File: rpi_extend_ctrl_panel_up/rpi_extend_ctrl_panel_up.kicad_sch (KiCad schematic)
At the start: 54 parts, among them J1 Raspberry_Pi_2_3, Q1 BC547, Q2 BC547, SW1 E-SWITCH-SW_Push_LED, SW2 RotaryEncoder, SW3 E-SWITCH-SW_Push_LED, SW4 RotaryEncoder, SW5 RotaryEncoder_Switch, SW6 on panel, U1 74HC14, U2 lcd_16x2_i2c

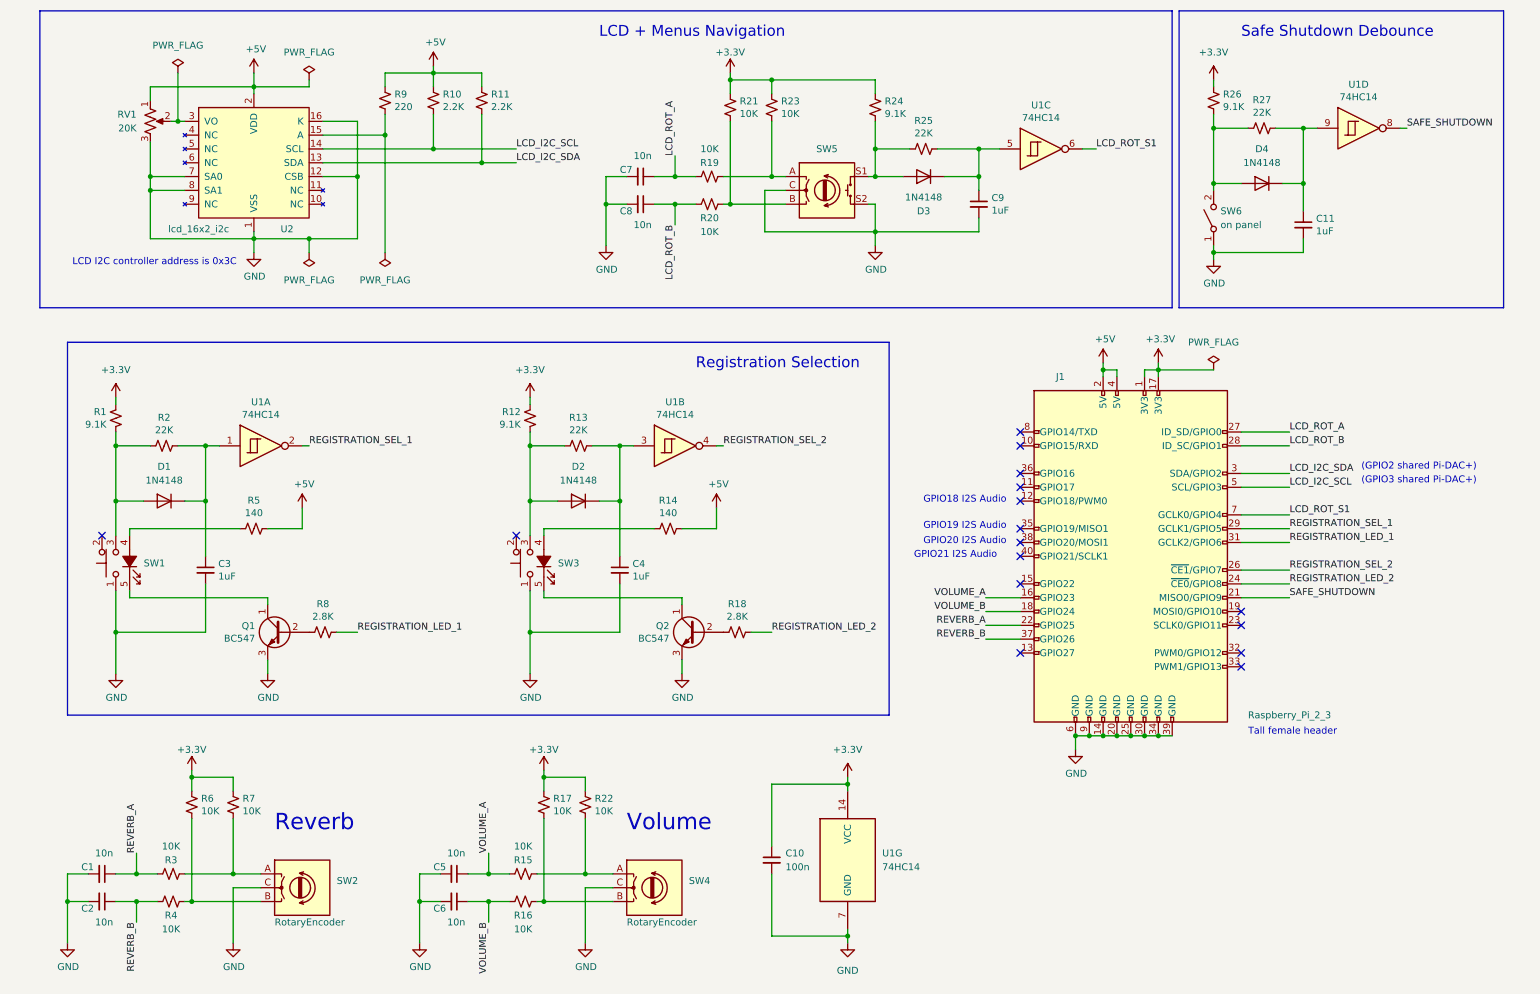
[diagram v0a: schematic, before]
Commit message: Rev 1.1: I2C pull-ups modified
SDA and SCL external pups (R10 and R11) discarded. Use Raspberry PI internal pups instead. Updating the PCB is not necessary.
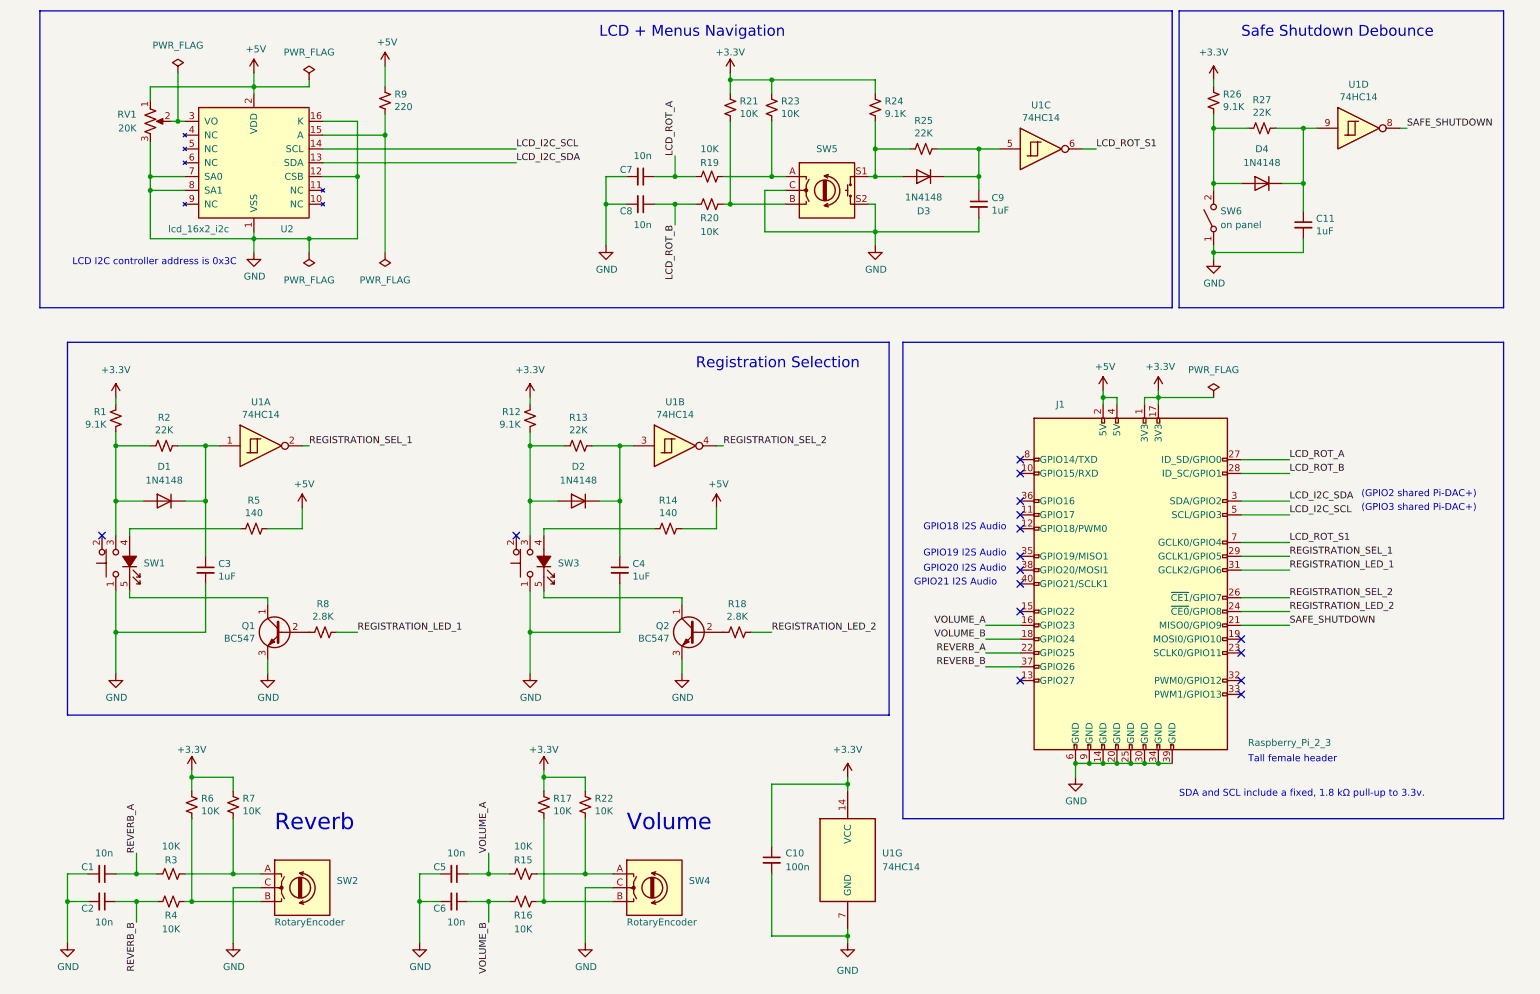
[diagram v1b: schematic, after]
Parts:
- removed R10, R11: 2.2K, Resistor_SMD:R_1206_3216Metric_Pad1.30x1.75mm_HandSolder, symbol Device:R_Small_US
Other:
- note added: "SDA and SCL include a fixed, 1.8 kΩ pull-up to 3.3v."
- moved on the sheet: J1

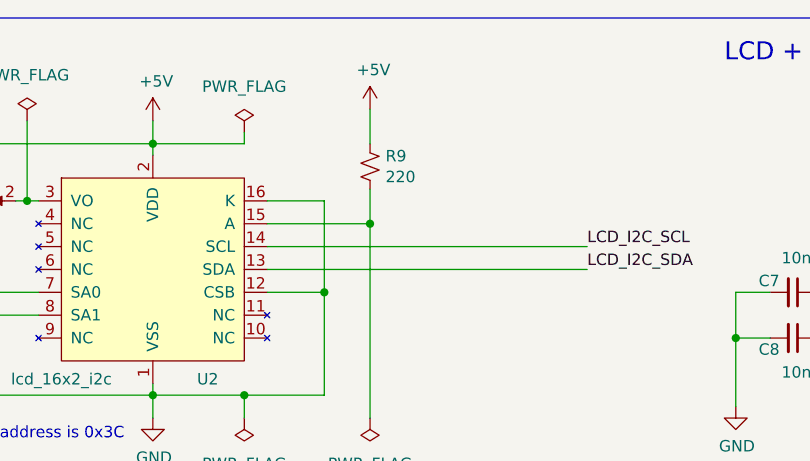
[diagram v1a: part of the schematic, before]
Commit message: Rev 1.1
I2C pull-ups discarded (use RPI I2C GPIO internal pull-ups). R9 value set to 51 Ohm.
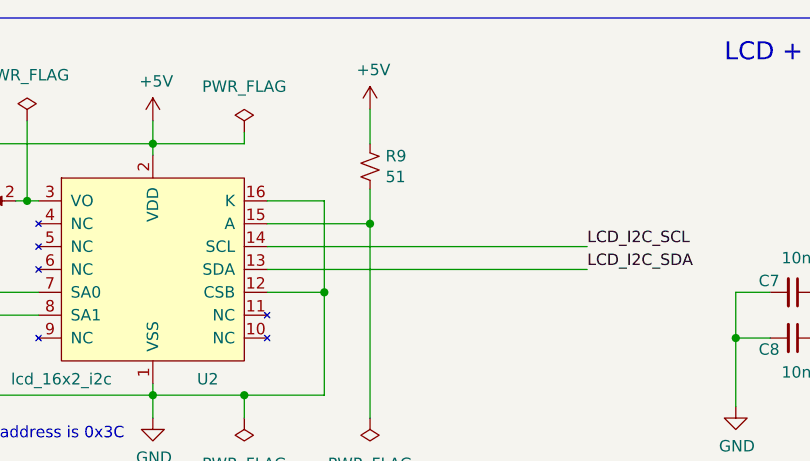
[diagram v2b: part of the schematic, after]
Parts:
- R9: value 220 -> 51
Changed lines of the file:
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@@
     (rev "1.1")
     (company "Picherie")
-    (comment 1 "Rev 1.1: SDA and SCL external pups (R10 and R11) discarded. Use Rpi internal pups instead.")
+    (comment 1 "SDA and SCL external pups (R10 and R11) discarded. Use Rpi internal pups instead.")
+    (comment 2 "R9 = 220 replaced with 51")
   )
   (junction (at 118.11 49.53) (diameter 0) (color 0 0 0 0)
@@
       (effects (font (size 1.27 1.27)) (justify left))
     )
-    (property "Value" "220" (id 1) (at 79.1972 31.623 0)
+    (property "Value" "51" (id 1) (at 79.1972 31.623 0)
       (effects (font (size 1.27 1.27)) (justify left))
     )
@@
     )
     (path "/00000000-0000-0000-0000-000061ba4973"
-      (reference "R9") (unit 1) (value "220") (footprint "Resistor_SMD:R_1206_3216Metric_Pad1.30x1.75mm_HandSolder")
+      (reference "R9") (unit 1) (value "51") (footprint "Resistor_SMD:R_1206_3216Metric_Pad1.30x1.75mm_HandSolder")
     )
     (path "/a9f36509-ce44-4e7e-bf3d-d4d8c7f2a8d8"

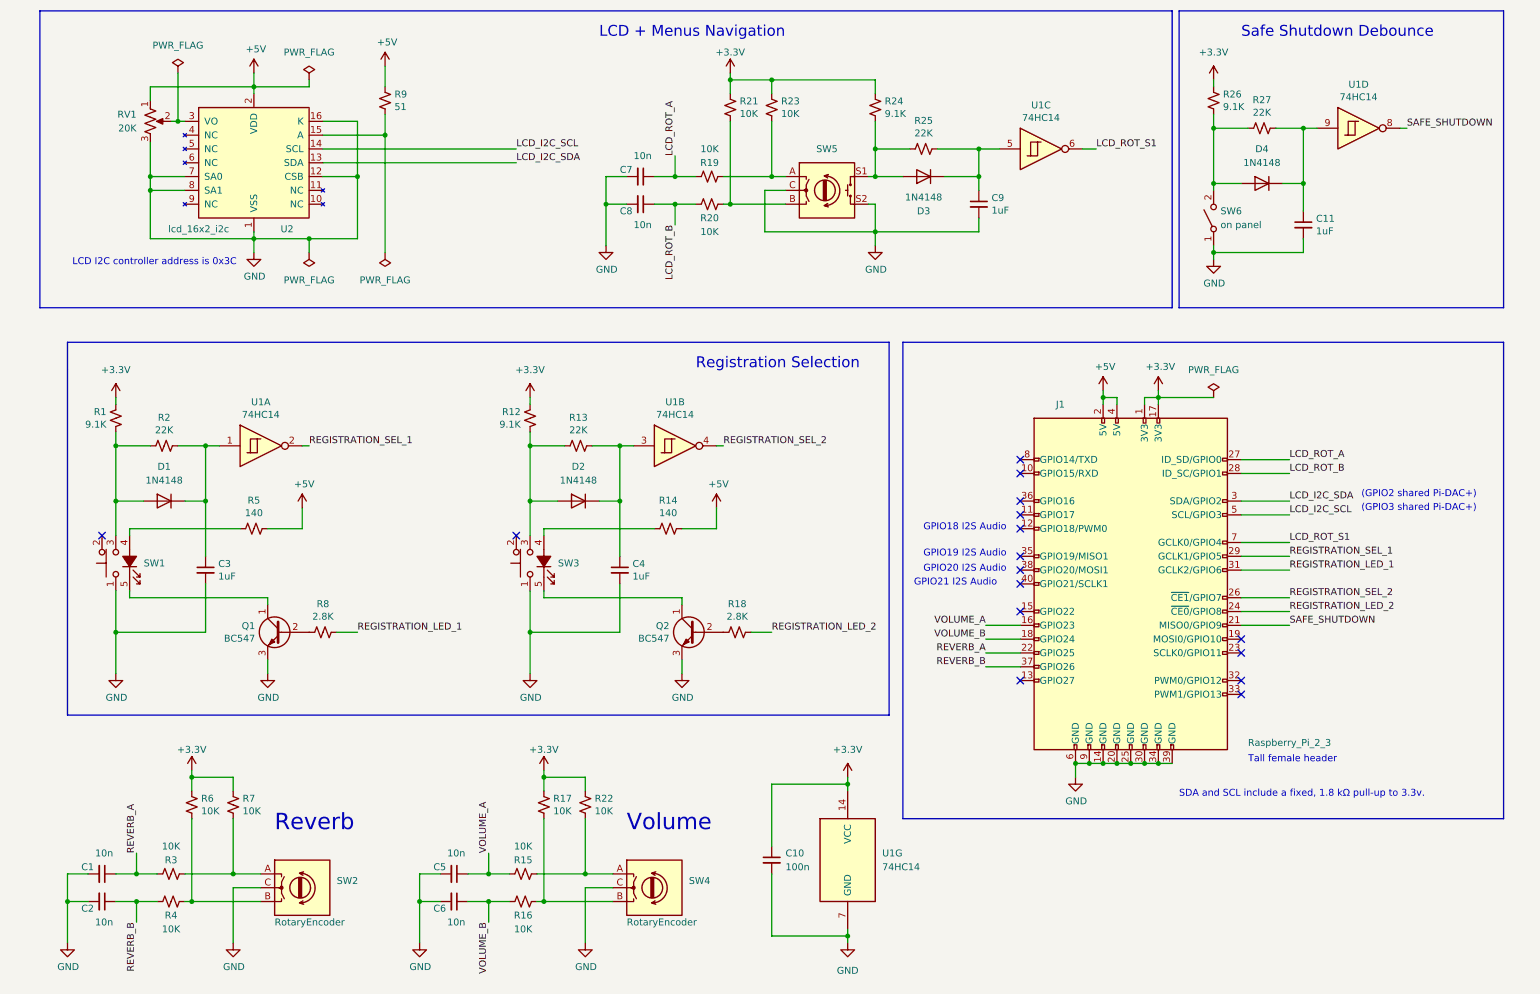
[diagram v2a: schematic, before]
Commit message: Rotary encoders debounce circuit simplified
V1.1
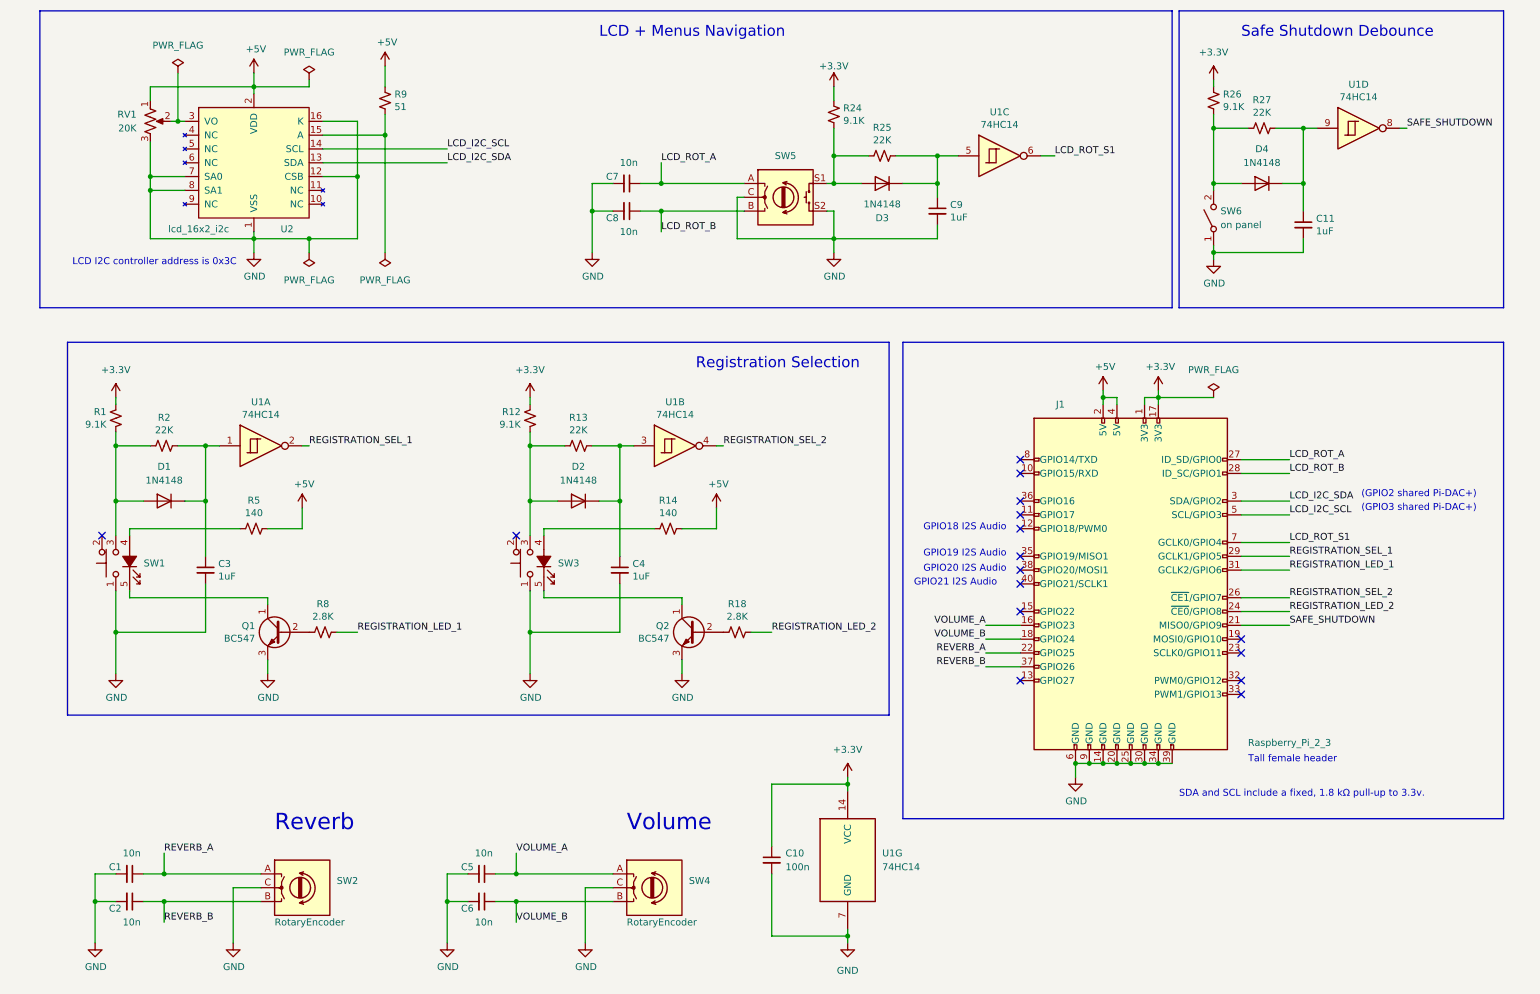
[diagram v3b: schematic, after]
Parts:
- removed R15, R16, R17, R19, R20, R21, R22, R23, R3, R4, R6, R7: 10K, Resistor_SMD:R_1206_3216Metric_Pad1.30x1.75mm_HandSolder, symbol Device:R_Small_US
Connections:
- net LCD_ROT_A: now also SW5.A
- net LCD_ROT_B: now also SW5.B
- net REVERB_A: now also SW2.A
- net REVERB_B: now also SW2.B
- net VOLUME_A: now also SW4.A
- net VOLUME_B: now also SW4.B
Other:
- moved on the sheet: C1, C2, C5, C6, C7, C8, C9, D3, R24, R25, SW5, U1C
